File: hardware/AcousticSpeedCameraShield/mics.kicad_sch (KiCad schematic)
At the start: 1 part, among them J1 Conn_01x05_Socket

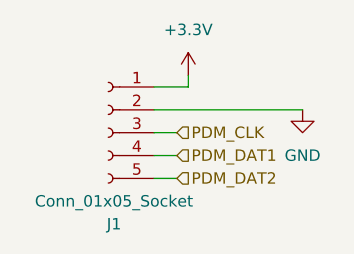
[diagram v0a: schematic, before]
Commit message: update MCU pin assignments
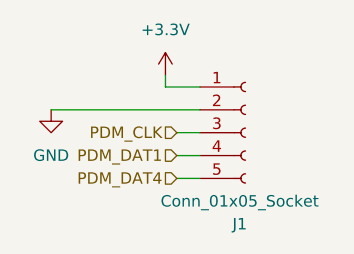
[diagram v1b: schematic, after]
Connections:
- net PDM_DAT2 renamed PDM_DAT4
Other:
- title: (none) -> Interfejs Mikrofonów
- moved on the sheet: J1
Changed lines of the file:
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@@
 	(paper "A4")
 	(title_block
+		(title "Interfejs Mikrofonów")
+		(date "2026-09-20")
 		(rev "1.0")
 		(comment 1 "Kinga Olszewska")
@@
 	(wire
 		(pts
-			(xy 144.78 97.79) (xy 147.32 97.79)
-		)
-		(stroke
-			(width 0)
-			(type default)
-		)
-	)
-	(wire
-		(pts
-			(xy 144.78 92.71) (xy 161.29 92.71)
-		)
-		(stroke
-			(width 0)
-			(type default)
-		)
-	)
-	(wire
-		(pts
-			(xy 144.78 90.17) (xy 148.59 90.17)
-		)
-		(stroke
-			(width 0)
-			(type default)
-		)
-	)
-	(wire
-		(pts
-			(xy 148.59 90.17) (xy 148.59 88.9)
-		)
-		(stroke
-			(width 0)
-			(type default)
-		)
-	)
-	(wire
-		(pts
-			(xy 144.78 100.33) (xy 147.32 100.33)
-		)
-		(stroke
-			(width 0)
-			(type default)
-		)
-	)
-	(wire
-		(pts
-			(xy 144.78 95.25) (xy 147.32 95.25)
+			(xy 149.86 97.79) (xy 147.32 97.79)
+		)
+		(stroke
+			(width 0)
+			(type default)
+		)
+	)
+	(wire
+		(pts
+			(xy 149.86 92.71) (xy 133.35 92.71)
+		)
+		(stroke
+			(width 0)
+			(type default)
+		)
+	)
+	(wire
+		(pts
+			(xy 149.86 90.17) (xy 146.05 90.17)
+		)
+		(stroke
+			(width 0)
+			(type default)
+		)
+	)
+	(wire
+		(pts
+			(xy 146.05 90.17) (xy 146.05 88.9)
+		)
+		(stroke
+			(width 0)
+			(type default)
+		)
+	)
+	(wire
+		(pts
+			(xy 149.86 100.33) (xy 147.32 100.33)
+		)
+		(stroke
+			(width 0)
+			(type default)
+		)
+	)
+	(wire
+		(pts
+			(xy 149.86 95.25) (xy 147.32 95.25)
 		)
 		(stroke
@@
 	(hierarchical_label "PDM_DAT1"
 		(shape input)
-		(at 147.32 97.79 0)
+		(at 147.32 97.79 180)
 		(effects
 			(font
 				(size 1.27 1.27)
 			)
-			(justify left)
-		)
-	)
-	(hierarchical_label "PDM_DAT2"
+			(justify right)
+		)
+	)
+	(hierarchical_label "PDM_DAT4"
 		(shape input)
-		(at 147.32 100.33 0)
+		(at 147.32 100.33 180)
 		(effects
 			(font
 				(size 1.27 1.27)
 			)
-			(justify left)
+			(justify right)
 		)
 	)
 	(hierarchical_label "PDM_CLK"
 		(shape input)
-		(at 147.32 95.25 0)
+		(at 147.32 95.25 180)
 		(effects
 			(font
 				(size 1.27 1.27)
 			)
-			(justify left)
+			(justify right)
 		)
 	)
 	(symbol
 		(lib_id "power:+3.3V")
-		(at 148.59 88.9 0)
+		(at 146.05 88.9 0)
+		(mirror y)
 		(unit 1)
 		(body_style 1)
@@
 		(fields_autoplaced yes)
 		(property "Reference" "#PWR029"
-			(at 148.59 92.71 0)
+			(at 146.05 92.71 0)
 			(hide yes)
 			(show_name no)
@@
 		)
 		(property "Value" "+3.3V"
-			(at 148.59 83.82 0)
+			(at 146.05 83.82 0)
 			(show_name no)
 			(do_not_autoplace no)
@@
 		)
 		(property "Footprint" ""
-			(at 148.59 88.9 0)
+			(at 146.05 88.9 0)
 			(hide yes)
 			(show_name no)
@@
 		)
 		(property "Datasheet" ""
-			(at 148.59 88.9 0)
+			(at 146.05 88.9 0)
 			(hide yes)
 			(show_name no)
@@
 		)
 		(property "Description" "Power symbol creates a global label with name \"+3.3V\""
-			(at 148.59 88.9 0)
+			(at 146.05 88.9 0)
 			(hide yes)
 			(show_name no)
@@
 	(symbol
 		(lib_id "power:GND")
-		(at 161.29 92.71 0)
+		(at 133.35 92.71 0)
+		(mirror y)
 		(unit 1)
 		(body_style 1)
@@
 		(fields_autoplaced yes)
 		(property "Reference" "#PWR030"
-			(at 161.29 99.06 0)
+			(at 133.35 99.06 0)
 			(hide yes)
 			(show_name no)
@@
 		)
 		(property "Value" "GND"
-			(at 161.29 97.79 0)
+			(at 133.35 97.79 0)
 			(show_name no)
 			(do_not_autoplace no)
@@
 		)
 		(property "Footprint" ""
-			(at 161.29 92.71 0)
+			(at 133.35 92.71 0)
 			(hide yes)
 			(show_name no)
@@
 		)
 		(property "Datasheet" ""
-			(at 161.29 92.71 0)
+			(at 133.35 92.71 0)
 			(hide yes)
 			(show_name no)
@@
 		)
 		(property "Description" "Power symbol creates a global label with name \"GND\" , ground"
-			(at 161.29 92.71 0)
+			(at 133.35 92.71 0)
 			(hide yes)
 			(show_name no)
@@
 	(symbol
 		(lib_id "Connector:Conn_01x05_Socket")
-		(at 139.7 95.25 0)
-		(mirror y)
+		(at 154.94 95.25 0)
 		(unit 1)
 		(body_style 1)
@@
 		(dnp no)
 		(property "Reference" "J1"
-			(at 140.335 105.41 0)
+			(at 154.305 105.41 0)
 			(show_name no)
 			(do_not_autoplace no)
@@
 		)
 		(property "Value" "Conn_01x05_Socket"
-			(at 140.335 102.87 0)
+			(at 154.305 102.87 0)
 			(show_name no)
 			(do_not_autoplace no)
@@
 		)
 		(property "Footprint" ""
-			(at 139.7 95.25 0)
+			(at 154.94 95.25 0)
 			(hide yes)
 			(show_name no)
@@
 		)
 		(property "Datasheet" ""
-			(at 139.7 95.25 0)
+			(at 154.94 95.25 0)
 			(hide yes)
 			(show_name no)
@@
 		)
 		(property "Description" "Generic connector, single row, 01x05, script generated"
-			(at 139.7 95.25 0)
-			(hide yes)
-			(show_name no)
+			(at 154.94 95.25 0)
+			(hide yes)
+			(show_name no)
